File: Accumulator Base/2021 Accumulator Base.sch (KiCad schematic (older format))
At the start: 53 parts, among them J1 Jumper, J10 Inverter&Motor, J11 Jumper, J12 EnergyMeter-OUT, J13 Dash, J14 Jumper, J15 Jumper, J16 Reset button, J17 Inverter-, J18 Jumper, J19 EnergyMeter-IN, J2 BMB, J3 TSMP, J4 Inv&Bat+, J5 Peripherals, J7 Interlocks, J8 Main LV, J9 AIRs, Q3 Q_NMOS_GDS, Q4 Q_NMOS_GDS, Q6 Q_NMOS_GDS, Q7 Q_NMOS_GDS, Q8 Q_NMOS_GDS, U1 74HC86, U2 IMD, U3 SDC-CUFR-Full-Library, U5 PWR_Transducer, U8 AIL&TSAL

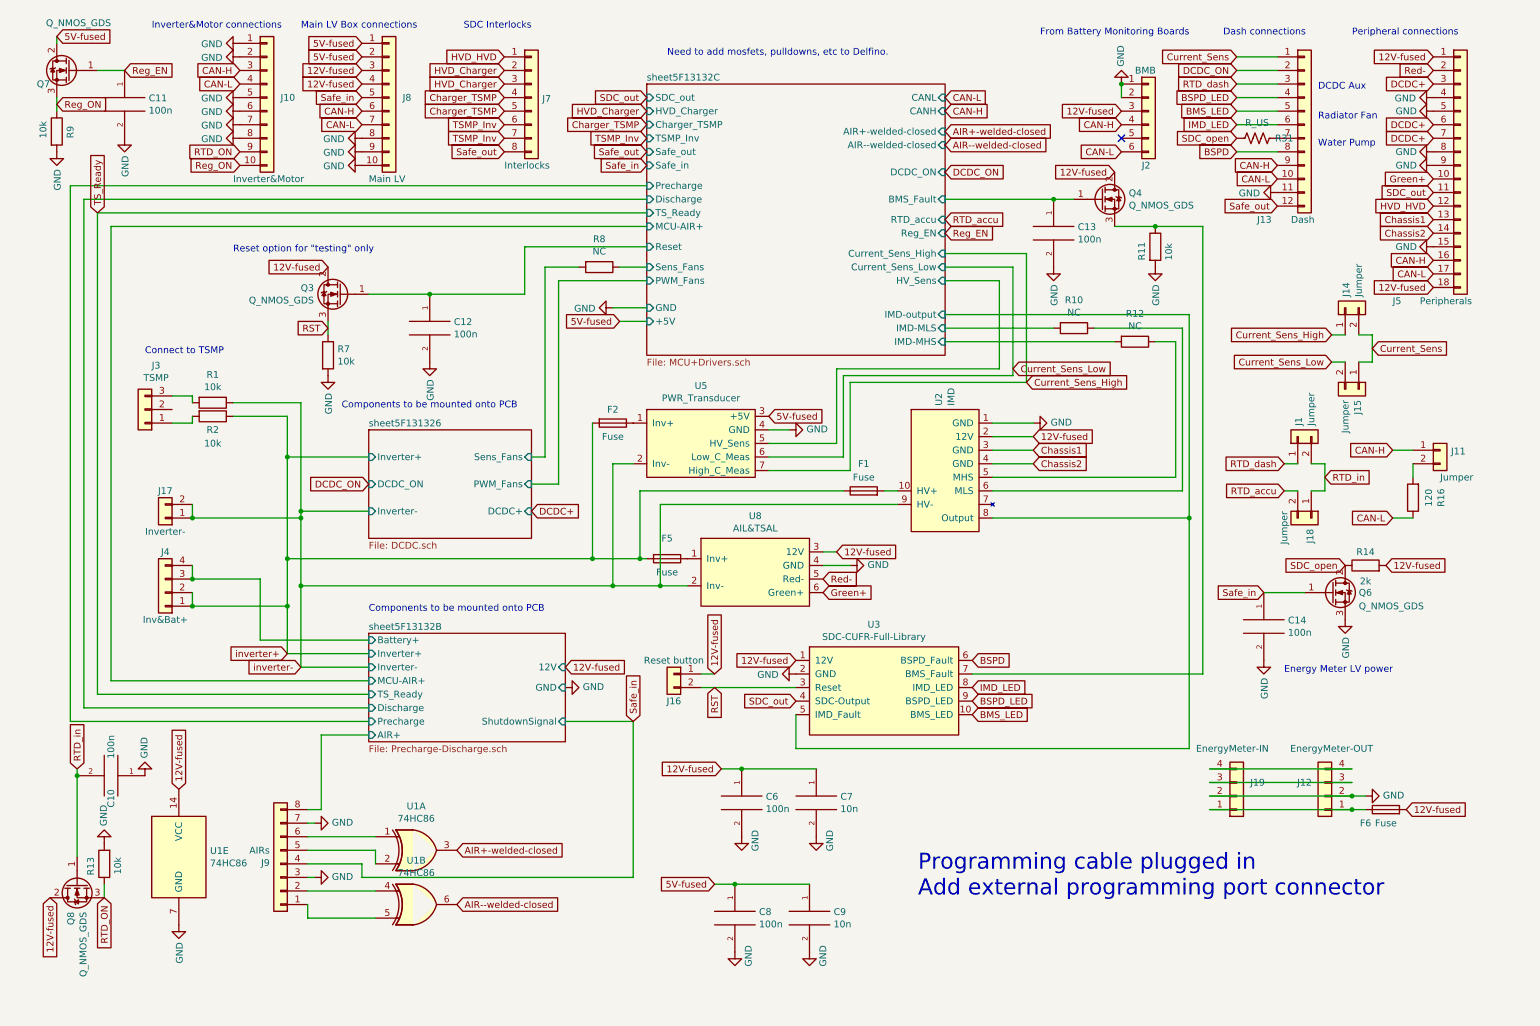
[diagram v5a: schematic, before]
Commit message: fp-lib-table files unignored and pull-down resistors added on NMOS gates in Base PCB
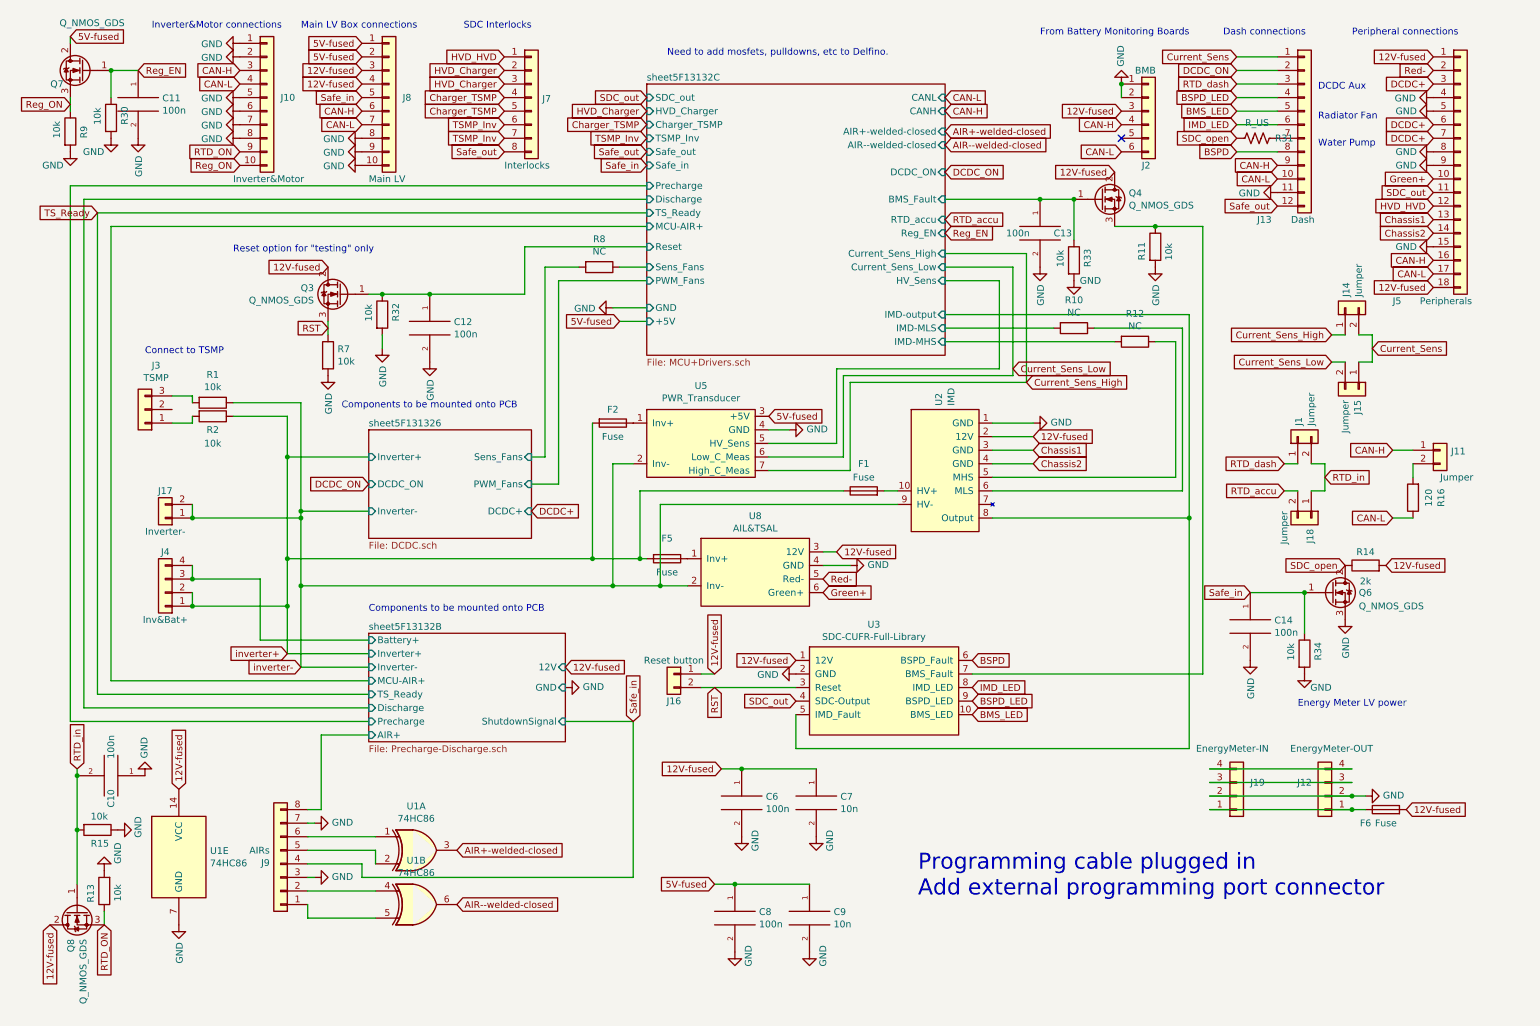
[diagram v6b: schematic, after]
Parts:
- added R15, R30, R32, R33, R34: 10k, Resistor_SMD:R_1206_3216Metric, symbol Device:R
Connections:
- net GND: now also R15.1, R30.2, R32.2, R33.2, R34.2
- net RTD_in: now also R15.2
- net Reg_EN: now also R30.1
- net Safe_in: now also R34.1
- net sheet5F13132C/BMS_Fault: now also R33.1
- net sheet5F13132C/Reset: now also R32.1
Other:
- moved on the sheet: C11, C13, C14, Q7, Q8, R13, R9

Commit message: Base PCB finished with traces
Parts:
- removed R34: 10k, Resistor_SMD:R_1206_3216Metric, symbol Device:R
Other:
- moved on the sheet: C14, Q6, R14
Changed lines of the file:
@@
 L Device:Q_NMOS_GDS Q?
 U 1 1 5F23AD1F
-P 10150 4750
+P 10200 4750
 AR Path="/5F13140A/5F23AD1F" Ref="Q?"  Part="1"
 AR Path="/5F23AD1F" Ref="Q6"  Part="1"
-F 0 "Q6" H 10350 4750 50  0000 L CNN
-F 1 "Q_NMOS_GDS" H 10350 4650 50  0000 L CNN
-F 2 "Package_TO_SOT_SMD:TO-252-2" H 10350 4850 50  0001 C CNN
-F 3 "~" H 10150 4750 50  0001 C CNN
-	1    10150 4750
+F 0 "Q6" H 10400 4750 50  0000 L CNN
+F 1 "Q_NMOS_GDS" H 10400 4650 50  0000 L CNN
+F 2 "Package_TO_SOT_SMD:TO-252-2" H 10400 4850 50  0001 C CNN
+F 3 "~" H 10200 4750 50  0001 C CNN
+	1    10200 4750
 	1    0    0    -1
 $EndComp
@@
 L power:GND #PWR?
 U 1 1 5F25E623
-P 10250 4950
+P 10300 4950
 AR Path="/5E8356A3/5F25E623" Ref="#PWR?"  Part="1"
 AR Path="/5F25E623" Ref="#PWR0102"  Part="1"
-F 0 "#PWR0102" H 10250 4700 50  0001 C CNN
-F 1 "GND" V 10255 4822 50  0000 R CNN
-F 2 "" H 10250 4950 50  0001 C CNN
-F 3 "" H 10250 4950 50  0001 C CNN
-	1    10250 4950
+F 0 "#PWR0102" H 10300 4700 50  0001 C CNN
+F 1 "GND" V 10305 4822 50  0000 R CNN
+F 2 "" H 10300 4950 50  0001 C CNN
+F 3 "" H 10300 4950 50  0001 C CNN
+	1    10300 4950
 	1    0    0    -1
 $EndComp
@@
 L Device:R R?
 U 1 1 5F28079E
-P 10400 4550
+P 10450 4550
 AR Path="/5E8356A3/5F28079E" Ref="R?"  Part="1"
 AR Path="/5F28079E" Ref="R14"  Part="1"
-F 0 "R14" V 10500 4550 50  0000 C CNN
-F 1 "2k" V 10284 4550 50  0000 C CNN
-F 2 "Resistor_SMD:R_1206_3216Metric" V 10330 4550 50  0001 C CNN
-F 3 "~" H 10400 4550 50  0001 C CNN
-	1    10400 4550
+F 0 "R14" V 10550 4550 50  0000 C CNN
+F 1 "2k" V 10334 4550 50  0000 C CNN
+F 2 "Resistor_SMD:R_1206_3216Metric" V 10380 4550 50  0001 C CNN
+F 3 "~" H 10450 4550 50  0001 C CNN
+	1    10450 4550
 	0    -1   -1   0
 $EndComp
-Text GLabel 10550 4550 2    50   Input ~ 0
+Text GLabel 10600 4550 2    50   Input ~ 0
 12V-fused
-Text GLabel 10250 4550 0    50   Input ~ 0
+Text GLabel 10300 4550 0    50   Input ~ 0
 SDC_open
 Text GLabel 4900 2750 0    50   Input ~ 0
@@
 Text GLabel 9450 1400 0    50   Input ~ 0
 SDC_open
-Text GLabel 9550 4750 0    50   Input ~ 0
+Text GLabel 9600 4750 0    50   Input ~ 0
 Safe_in
 $Comp
@@
 Text GLabel 10700 6350 2    50   Input ~ 0
 12V-fused
-Text Notes 9900 5600 0    50   ~ 0
+Text Notes 9950 5450 0    50   ~ 0
 Energy Meter LV power
 Text GLabel 7900 3200 2    50   Input ~ 0
@@
 L pspice:C C14
 U 1 1 5F4BB322
-P 9550 5000
-F 0 "C14" H 9728 5046 50  0000 L CNN
-F 1 "100n" H 9728 4955 50  0000 L CNN
-F 2 "Capacitor_SMD:C_0805_2012Metric" H 9550 5000 50  0001 C CNN
-F 3 "~" H 9550 5000 50  0001 C CNN
-	1    9550 5000
+P 9800 5000
+F 0 "C14" H 9978 5046 50  0000 L CNN
+F 1 "100n" H 9978 4955 50  0000 L CNN
+F 2 "Capacitor_SMD:C_0805_2012Metric" H 9800 5000 50  0001 C CNN
+F 3 "~" H 9800 5000 50  0001 C CNN
+	1    9800 5000
 	1    0    0    -1
 $EndComp
@@
 L power:GND #PWR?
 U 1 1 5F4BC1FA
-P 9550 5250
+P 9800 5250
 AR Path="/5E8356A3/5F4BC1FA" Ref="#PWR?"  Part="1"
 AR Path="/5F4BC1FA" Ref="#PWR0128"  Part="1"
-F 0 "#PWR0128" H 9550 5000 50  0001 C CNN
-F 1 "GND" V 9555 5122 50  0000 R CNN
-F 2 "" H 9550 5250 50  0001 C CNN
-F 3 "" H 9550 5250 50  0001 C CNN
-	1    9550 5250
+F 0 "#PWR0128" H 9800 5000 50  0001 C CNN
+F 1 "GND" V 9805 5122 50  0000 R CNN
+F 2 "" H 9800 5250 50  0001 C CNN
+F 3 "" H 9800 5250 50  0001 C CNN
+	1    9800 5250
 	1    0    0    -1
 $EndComp
@@
 	0    -1   -1   0
 $EndComp
-$Comp
-L Device:R R?
-U 1 1 5F4469E9
-P 9950 5200
-AR Path="/5F13151C/5F4469E9" Ref="R?"  Part="1"
-AR Path="/5F4469E9" Ref="R34"  Part="1"
-F 0 "R34" V 10050 5150 50  0000 L CNN
-F 1 "10k" V 9850 5150 50  0000 L CNN
-F 2 "Resistor_SMD:R_1206_3216Metric" V 9880 5200 50  0001 C CNN
-F 3 "~" H 9950 5200 50  0001 C CNN
-	1    9950 5200
-	1    0    0    -1
-$EndComp
-$Comp
-L power:GND #PWR?
-U 1 1 5F4483BC
-P 9950 5350
-AR Path="/5E8356A3/5F4483BC" Ref="#PWR?"  Part="1"
-AR Path="/5F4483BC" Ref="#PWR0137"  Part="1"
-F 0 "#PWR0137" H 9950 5100 50  0001 C CNN
-F 1 "GND" H 10150 5250 50  0000 R CNN
-F 2 "" H 9950 5350 50  0001 C CNN
-F 3 "" H 9950 5350 50  0001 C CNN
-	1    9950 5350
-	1    0    0    -1
-$EndComp
-Wire Wire Line
-	9550 4750 9950 4750
-Wire Wire Line
-	9950 5050 9950 4750
-Connection ~ 9950 4750
+Wire Wire Line
+	9600 4750 9800 4750
+Connection ~ 9800 4750
+Wire Wire Line
+	9800 4750 10000 4750
 $EndSCHEMATC

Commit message: Vibration damping fasteners added to all PCB shields
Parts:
- removed U3: SDC-CUFR-Full-Library, CUFR-Full-Footprint-Library:SDC_Module2021, symbol CUFR-Full-Library:SDC
- added U3: SDC_9-8-20, SDC:SDC_9-8-20, symbol SDC_9-8-20:SDC_9-8-20
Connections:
- wire segments 170 -> 172
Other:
- moved on the sheet: J16
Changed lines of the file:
@@
 L power:GND #PWR?
 U 1 1 5F1313E0
-P 6200 5350
+P 7350 4900
 AR Path="/5E8356A3/5F1313E0" Ref="#PWR?"  Part="1"
 AR Path="/5F1313E0" Ref="#PWR07"  Part="1"
-F 0 "#PWR07" H 6200 5100 50  0001 C CNN
-F 1 "GND" V 6205 5222 50  0000 R CNN
-F 2 "" H 6200 5350 50  0001 C CNN
-F 3 "" H 6200 5350 50  0001 C CNN
-	1    6200 5350
-	0    1    1    0
-$EndComp
-Text GLabel 5600 5350 1    50   Input ~ 0
-12V-fused
+F 0 "#PWR07" H 7350 4650 50  0001 C CNN
+F 1 "GND" V 7355 4772 50  0000 R CNN
+F 2 "" H 7350 4900 50  0001 C CNN
+F 3 "" H 7350 4900 50  0001 C CNN
+	1    7350 4900
+	0    1    1    0
+$EndComp
 Wire Wire Line
 	3050 3750 2450 3750
@@
 	2550 4700 4850 4700
 Connection ~ 5200 4700
-Text GLabel 7500 5250 2    50   Input ~ 0
+Text GLabel 7350 5400 0    50   Input ~ 0
 BSPD
 Wire Wire Line
@@
 Wire Wire Line
 	4900 2350 5100 2350
-Text GLabel 6200 5550 0    50   Input ~ 0
+Text GLabel 7350 5100 0    50   Input ~ 0
 SDC_out
 Text GLabel 5100 1100 0    50   Input ~ 0
@@
 Text Notes 2550 600  0    50   ~ 0
 Main LV Box connections
-Wire Wire Line
-	9200 2050 9200 5350
 $Comp
 L power:GND #PWR?
@@
 Wire Wire Line
 	2250 4650 2250 5100
-Text GLabel 5600 5450 3    50   Input ~ 0
-RST
 $Comp
 L Device:Q_NMOS_GDS Q?
@@
 Text GLabel 7300 1650 2    50   Input ~ 0
 DCDC_ON
-Text GLabel 6200 5250 0    50   Input ~ 0
+Text GLabel 7350 4800 0    50   Input ~ 0
 12V-fused
 Text GLabel 3000 1000 0    50   Input ~ 0
@@
 Text GLabel 2100 1600 0    50   Input ~ 0
 Reg_ON
-$Comp
-L CUFR-Full-Library:SDC U?
-U 1 1 5F36299A
-P 6800 5250
-AR Path="/5E8356A3/5EF3856E/5F36299A" Ref="U?"  Part="1"
-AR Path="/5F1313D9/5F36299A" Ref="U?"  Part="1"
-AR Path="/5F36299A" Ref="U3"  Part="1"
-F 0 "U3" H 6775 5515 50  0000 C CNN
-F 1 "SDC-CUFR-Full-Library" H 6775 5424 50  0000 C CNN
-F 2 "CUFR-Full-Footprint-Library:SDC_Module2021" V 6250 5400 50  0001 C CNN
-F 3 "" V 6250 5400 50  0001 C CNN
-	1    6800 5250
-	1    0    0    -1
-$EndComp
-Wire Wire Line
-	5500 5350 5600 5350
-Wire Wire Line
-	6200 5450 5500 5450
-Wire Wire Line
-	6200 5650 6200 5900
-Wire Wire Line
-	7500 5350 9200 5350
-Wire Wire Line
-	9100 5900 9100 4200
 Connection ~ 9100 4200
 Wire Wire Line
 	7650 4200 9100 4200
-Wire Wire Line
-	6200 5900 9100 5900
-$Comp
-L Connector_Generic:Conn_01x02 J?
-U 1 1 5F26A6E8
-P 5300 5350
-AR Path="/5E8356A3/5F26A6E8" Ref="J?"  Part="1"
-AR Path="/5F26A6E8" Ref="J16"  Part="1"
-F 0 "J16" H 5300 5150 50  0000 C CNN
-F 1 "Reset button" H 5300 5450 50  0000 C CNN
-F 2 "Connector_Molex:Molex_Micro-Fit_3.0_43650-0215_1x02_P3.00mm_Vertical" H 5300 5350 50  0001 C CNN
-F 3 "~" H 5300 5350 50  0001 C CNN
-	1    5300 5350
-	-1   0    0    -1
-$EndComp
-Text GLabel 7500 5550 2    50   Input ~ 0
+Text GLabel 8500 4800 2    50   Input ~ 0
 BSPD_LED
-Text GLabel 7500 5450 2    50   Input ~ 0
+Text GLabel 8500 4700 2    50   Input ~ 0
 IMD_LED
-Text GLabel 7500 5650 2    50   Input ~ 0
+Text GLabel 8500 4900 2    50   Input ~ 0
 BMS_LED
 $Comp
@@
 Wire Wire Line
 	9800 4750 10000 4750
+$Comp
+L SDC_9-8-20:SDC_9-8-20 U3
+U 1 1 5F5B0511
+P 7950 4500
+F 0 "U3" H 7925 4565 50  0000 C CNN
+F 1 "SDC_9-8-20" H 7925 4474 50  0000 C CNN
+F 2 "SDC:SDC_9-8-20" H 7950 4500 50  0001 C CNN
+F 3 "" H 7950 4500 50  0001 C CNN
+	1    7950 4500
+	1    0    0    -1
+$EndComp
+Text GLabel 7350 5200 0    50   Input ~ 0
+RST
+Wire Wire Line
+	9200 2050 9200 5800
+Wire Wire Line
+	7350 5500 7350 5700
+Wire Wire Line
+	7350 5700 9100 5700
+Wire Wire Line
+	9100 5700 9100 4200
+Wire Wire Line
+	9200 5800 7000 5800
+Wire Wire Line
+	7000 5800 7000 5300
+Wire Wire Line
+	7000 5300 7350 5300
+Text GLabel 6200 5450 1    50   Input ~ 0
+12V-fused
+Text GLabel 6200 5550 3    50   Input ~ 0
+RST
+Wire Wire Line
+	6100 5450 6200 5450
+$Comp
+L Connector_Generic:Conn_01x02 J?
+U 1 1 5F26A6E8
+P 5900 5450
+AR Path="/5E8356A3/5F26A6E8" Ref="J?"  Part="1"
+AR Path="/5F26A6E8" Ref="J16"  Part="1"
+F 0 "J16" H 5900 5250 50  0000 C CNN
+F 1 "Reset button" H 5900 5550 50  0000 C CNN
+F 2 "Connector_Molex:Molex_Micro-Fit_3.0_43650-0215_1x02_P3.00mm_Vertical" H 5900 5450 50  0001 C CNN
+F 3 "~" H 5900 5450 50  0001 C CNN
+	1    5900 5450
+	-1   0    0    -1
+$EndComp
+Wire Wire Line
+	6100 5550 6200 5550
+Text GLabel 7350 4700 0    50   Input ~ 0
+5V-fused
 $EndSCHEMATC
